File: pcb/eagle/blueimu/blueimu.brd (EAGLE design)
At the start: 50 x 73 mm, 26 parts, among them IC1 ICL7665CPA, IC2 ATMEGA328P, IC3 LP2950Z, J1 22-27-2021-02, Q1 IRL3803, Q2 7.3728MHz

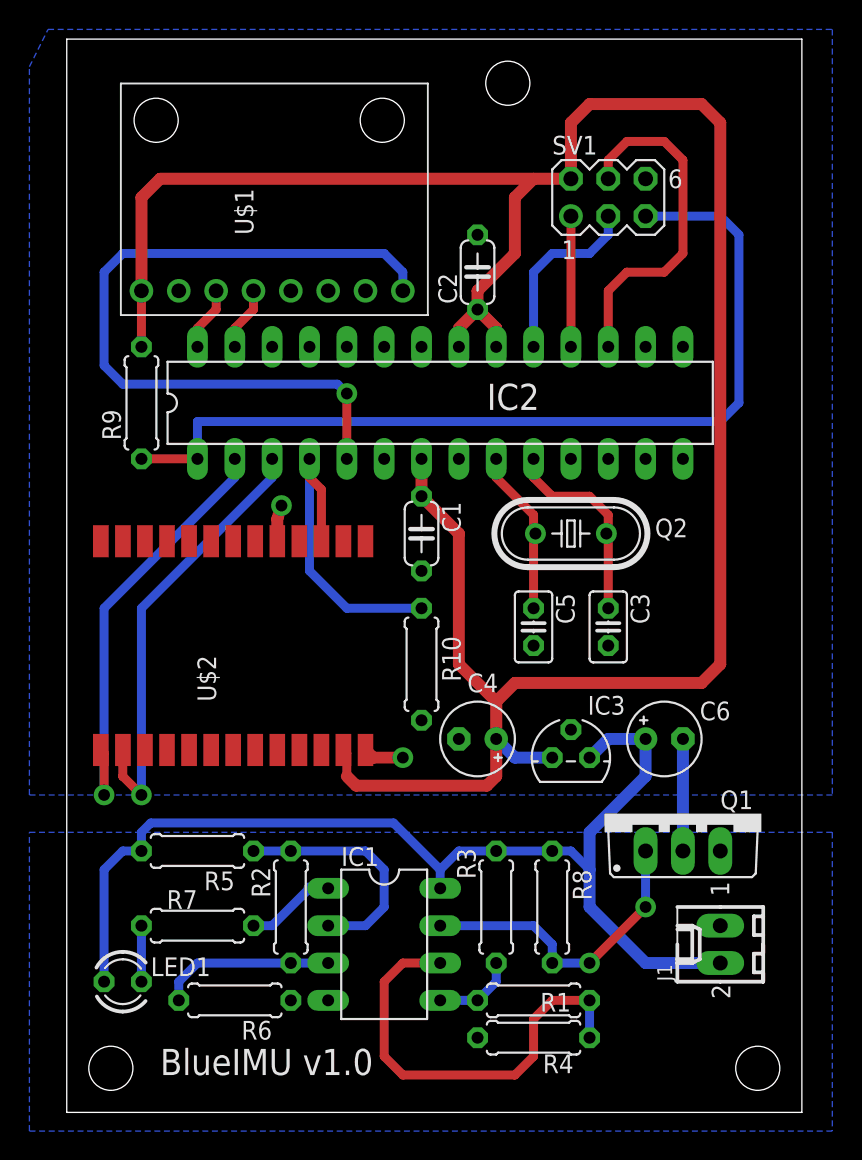
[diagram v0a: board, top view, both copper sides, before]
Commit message: Cosmetic changes to schematics and board layout
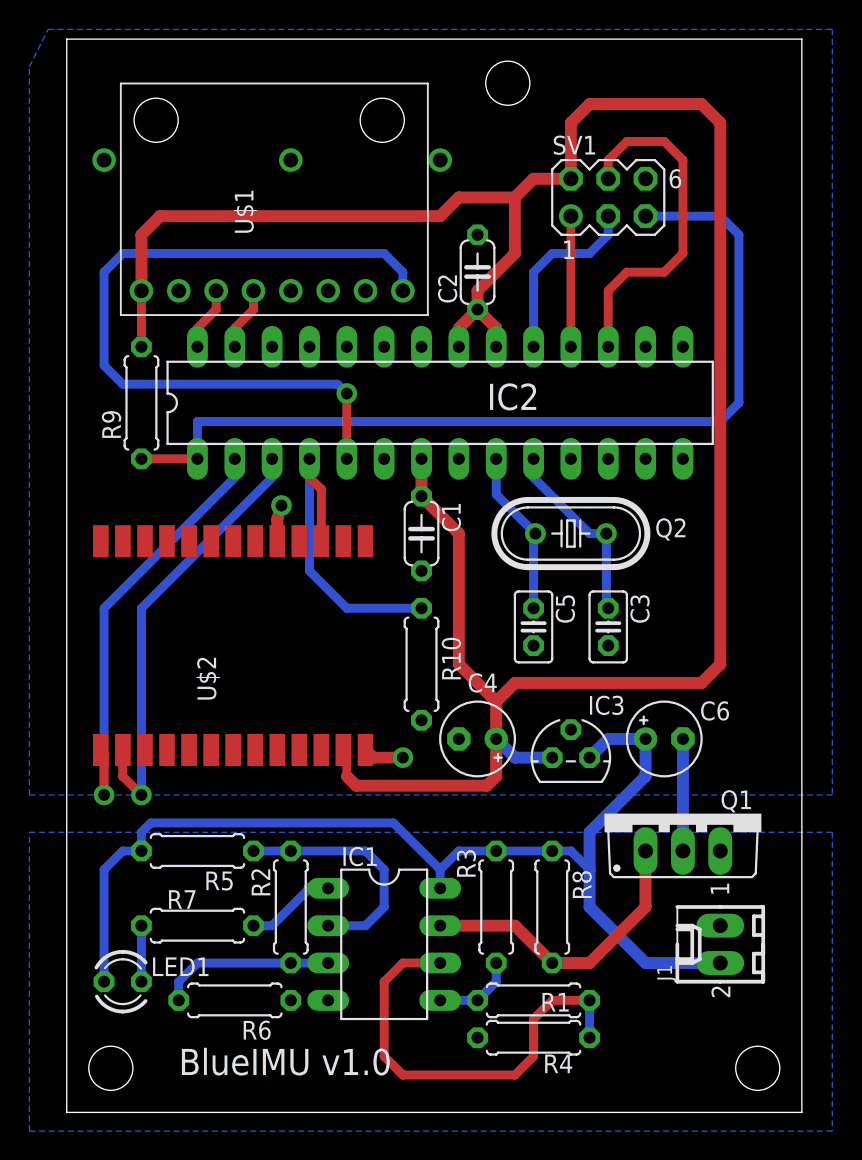
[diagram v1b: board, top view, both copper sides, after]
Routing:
- net +3V3: track 165.2 -> 162.0 mm
- net N$10: track 13.8 -> 12.9 mm
- net N$9: track 21.2 -> 20.4 mm, vias 2 -> 0
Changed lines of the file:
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@@
 <setting verticaltext="up"/>
 </settings>
-<grid distance="1270" unitdist="mic" unit="mil" style="lines" multiple="1" display="yes" altdistance="0.635" altunitdist="mm" altunit="mm"/>
+<grid distance="1.27" unitdist="mm" unit="mm" style="lines" multiple="1" display="yes" altdistance="0.635" altunitdist="mm" altunit="mm"/>
 <layers>
 <layer number="1" name="Top" color="4" fill="1" visible="yes" active="yes"/>
@@
 <hole x="3" y="3" drill="3"/>
 <hole x="47" y="3" drill="3"/>
-<circle x="47" y="3" radius="3" width="0" layer="42"/>
-<circle x="3" y="3" radius="3" width="0" layer="42"/>
+<circle x="47" y="3" radius="3.3" width="0" layer="42"/>
+<circle x="3" y="3" radius="3.3" width="0" layer="42"/>
 <hole x="30" y="70" drill="3"/>
-<circle x="30" y="70" radius="3" width="0" layer="42"/>
-<text x="6.35" y="2.54" size="1.778" layer="21">BlueIMU v1.0</text>
+<circle x="30" y="70" radius="3.3" width="0" layer="42"/>
+<text x="7.62" y="2.54" size="1.778" layer="21">BlueIMU v1.0</text>
 </plain>
 <attributes>
@@
 <contactref element="Q1" pad="G"/>
 <contactref element="R8" pad="2"/>
-<wire x1="25.4" y1="12.7" x2="31.75" y2="12.7" width="0.6096" layer="16"/>
-<wire x1="31.75" y1="12.7" x2="33.02" y2="11.43" width="0.6096" layer="16"/>
-<wire x1="33.02" y1="11.43" x2="33.02" y2="10.16" width="0.6096" layer="16"/>
-<via x="35.56" y="10.16" extent="1-16" drill="0.8"/>
-<wire x1="33.02" y1="10.16" x2="35.56" y2="10.16" width="0.6096" layer="16"/>
-<via x="39.37" y="13.97" extent="1-16" drill="0.8"/>
-<wire x1="39.37" y1="17.78" x2="39.37" y2="13.97" width="0.6096" layer="16"/>
-<wire x1="35.56" y1="10.16" x2="39.37" y2="13.97" width="0.6096" layer="1"/>
+<wire x1="25.4" y1="12.7" x2="30.48" y2="12.7" width="0.8128" layer="1"/>
+<wire x1="30.48" y1="12.7" x2="33.02" y2="10.16" width="0.8128" layer="1"/>
+<wire x1="33.02" y1="10.16" x2="35.56" y2="10.16" width="0.8128" layer="1"/>
+<wire x1="35.56" y1="10.16" x2="39.37" y2="13.97" width="0.8128" layer="1"/>
+<wire x1="39.37" y1="13.97" x2="39.37" y2="17.78" width="0.8128" layer="1"/>
 </signal>
 <signal name="N$12">
@@
 <wire x1="30.48" y1="62.23" x2="30.48" y2="58.42" width="0.8128" layer="1"/>
 <wire x1="5.08" y1="55.88" x2="5.08" y2="52.07" width="0.6096" layer="1"/>
-<wire x1="5.08" y1="55.88" x2="5.08" y2="62.23" width="0.8128" layer="1"/>
-<wire x1="5.08" y1="62.23" x2="6.35" y2="63.5" width="0.8128" layer="1"/>
-<wire x1="6.35" y1="63.5" x2="31.75" y2="63.5" width="0.8128" layer="1"/>
 <wire x1="29.21" y1="25.4" x2="29.21" y2="22.86" width="0.8128" layer="1"/>
 <wire x1="29.21" y1="22.86" x2="28.575" y2="22.225" width="0.8128" layer="1"/>
@@
 <wire x1="27.94" y1="54.61" x2="29.21" y2="53.34" width="0.8128" layer="1"/>
 <wire x1="29.21" y1="53.34" x2="29.21" y2="52.07" width="0.8128" layer="1"/>
+<wire x1="25.4" y1="60.96" x2="6.35" y2="60.96" width="0.8128" layer="1"/>
+<wire x1="6.35" y1="60.96" x2="5.08" y2="59.69" width="0.8128" layer="1"/>
+<wire x1="5.08" y1="59.69" x2="5.08" y2="55.88" width="0.8128" layer="1"/>
+<wire x1="25.4" y1="60.96" x2="26.67" y2="62.23" width="0.8128" layer="1"/>
+<wire x1="26.67" y1="62.23" x2="30.48" y2="62.23" width="0.8128" layer="1"/>
 </signal>
 <signal name="TXD">
@@
 </signal>
 <signal name="N$15">
-<wire x1="31.75" y1="40.64" x2="29.21" y2="43.18" width="0.6096" layer="1"/>
 <contactref element="IC2" pad="9"/>
 <contactref element="Q2" pad="1"/>
 <contactref element="C5" pad="1"/>
-<wire x1="29.21" y1="43.18" x2="29.21" y2="44.45" width="0.6096" layer="1"/>
-<wire x1="31.75" y1="34.29" x2="31.75" y2="40.64" width="0.6096" layer="1"/>
-<wire x1="31.75" y1="40.64" x2="31.877" y2="39.37" width="0" layer="19" extent="1-1"/>
+<wire x1="31.877" y1="39.37" x2="31.75" y2="39.243" width="0.6096" layer="16"/>
+<wire x1="31.75" y1="39.243" x2="31.75" y2="34.29" width="0.6096" layer="16"/>
+<wire x1="31.877" y1="39.37" x2="29.21" y2="42.037" width="0.6096" layer="16"/>
+<wire x1="29.21" y1="42.037" x2="29.21" y2="44.45" width="0.6096" layer="16"/>
 </signal>
 <signal name="N$10">
-<wire x1="36.83" y1="40.64" x2="35.56" y2="41.91" width="0.6096" layer="1"/>
-<wire x1="35.56" y1="41.91" x2="33.02" y2="41.91" width="0.6096" layer="1"/>
 <contactref element="IC2" pad="10"/>
 <contactref element="Q2" pad="2"/>
 <contactref element="C3" pad="1"/>
-<wire x1="33.02" y1="41.91" x2="31.75" y2="43.18" width="0.6096" layer="1"/>
-<wire x1="31.75" y1="43.18" x2="31.75" y2="44.45" width="0.6096" layer="1"/>
-<wire x1="36.83" y1="34.29" x2="36.83" y2="40.64" width="0.6096" layer="1"/>
-<wire x1="36.83" y1="40.64" x2="36.703" y2="39.37" width="0" layer="19" extent="1-1"/>
+<wire x1="36.83" y1="34.29" x2="36.703" y2="34.417" width="0.6096" layer="16" curve="-90"/>
+<wire x1="36.703" y1="34.417" x2="36.703" y2="39.37" width="0.6096" layer="16"/>
+<wire x1="36.703" y1="39.37" x2="35.56" y2="39.37" width="0.6096" layer="16"/>
+<wire x1="35.56" y1="39.37" x2="31.75" y2="43.18" width="0.6096" layer="16"/>
+<wire x1="31.75" y1="43.18" x2="31.75" y2="44.45" width="0.6096" layer="16"/>
+</signal>
+<signal name="N$11">
+<via x="2.54" y="64.77" extent="1-16" drill="1" shape="octagon"/>
+</signal>
+<signal name="N$14">
+<via x="25.4" y="64.77" extent="1-16" drill="1" shape="octagon"/>
+</signal>
+<signal name="N$16">
+<via x="15.24" y="64.77" extent="1-16" drill="1" shape="octagon"/>
 </signal>
 </signals>

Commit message: Added capacitor. Added Gerber files.
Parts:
- added C7: 100nF, rcl:C050-024X044
- R8: value 1M -> 470k
- moved J1 1.27 mm to (44.5, 10.2)
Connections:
- net BAT-: now also C7.2
- net N$9: now also C7.1
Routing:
- net BAT+: track 74.1 -> 74.7 mm
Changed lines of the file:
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@@
 <attribute name="VALUE" x="11.176" y="13.2588" size="1.27" layer="27" ratio="10" rot="R180"/>
 </element>
-<element name="R8" library="rcl" package="0207/7" value="1M" x="33.02" y="13.97" rot="R270"/>
+<element name="R8" library="rcl" package="0207/7" value="470k" x="33.02" y="13.97" rot="R270"/>
 <element name="SV1" library="con-lstb" package="MA03-2" value="" x="36.83" y="62.23" smashed="yes">
 <attribute name="OC_NEWARK" value="unknown" x="36.83" y="62.23" size="1.778" layer="27" display="off"/>
@@
 <attribute name="VALUE" x="35.56" y="58.039" size="1.27" layer="27" ratio="10"/>
 </element>
-<element name="J1" library="con-molex" package="6410-02" value="22-27-2021-02" x="44.45" y="11.43" rot="R90">
-<attribute name="OC_NEWARK" value="unknown" x="44.45" y="11.43" size="1.778" layer="27" rot="R90" display="off"/>
-<attribute name="MPN" value="" x="44.45" y="11.43" size="1.778" layer="27" rot="R90" display="off"/>
-<attribute name="MF" value="" x="44.45" y="11.43" size="1.778" layer="27" rot="R90" display="off"/>
-<attribute name="OC_FARNELL" value="unknown" x="44.45" y="11.43" size="1.778" layer="27" rot="R90" display="off"/>
+<element name="J1" library="con-molex" package="6410-02" value="22-27-2021-02" x="44.45" y="10.16" rot="R90">
+<attribute name="OC_NEWARK" value="unknown" x="44.45" y="10.16" size="1.778" layer="27" rot="R90" display="off"/>
+<attribute name="MPN" value="" x="44.45" y="10.16" size="1.778" layer="27" rot="R90" display="off"/>
+<attribute name="MF" value="" x="44.45" y="10.16" size="1.778" layer="27" rot="R90" display="off"/>
+<attribute name="OC_FARNELL" value="unknown" x="44.45" y="10.16" size="1.778" layer="27" rot="R90" display="off"/>
 </element>
 <element name="IC2" library="atmel" package="DIL28-3" value="ATMEGA328P" x="25.4" y="48.26" smashed="yes">
@@
 <attribute name="VALUE" x="23.5712" y="32.766" size="1.27" layer="27" ratio="10" rot="R270"/>
 </element>
+<element name="C7" library="rcl" package="C050-024X044" value="100nF" x="41.91" y="14.605" smashed="yes">
+<attribute name="NAME" x="45.466" y="14.097" size="1.27" layer="25" ratio="10"/>
+<attribute name="VALUE" x="39.751" y="11.938" size="1.27" layer="27" ratio="10"/>
+</element>
 </elements>
 <signals>
@@
 <contactref element="C6" pad="+"/>
 <contactref element="IC3" pad="3"/>
-<wire x1="44.45" y1="10.16" x2="39.37" y2="10.16" width="0.8128" layer="16"/>
-<wire x1="39.37" y1="10.16" x2="35.56" y2="13.97" width="0.8128" layer="16"/>
+<wire x1="44.45" y1="8.89" x2="40.64" y2="8.89" width="0.8128" layer="16"/>
+<wire x1="40.64" y1="8.89" x2="35.56" y2="13.97" width="0.8128" layer="16"/>
 <wire x1="35.56" y1="13.97" x2="35.56" y2="16.51" width="0.8128" layer="16"/>
 <wire x1="35.56" y1="16.51" x2="34.29" y2="17.78" width="0.6096" layer="16"/>
@@
 </polygon>
 <contactref element="J1" pad="1"/>
+<contactref element="C7" pad="2"/>
 </signal>
 <signal name="N$3">
@@
 <wire x1="30.48" y1="12.7" x2="33.02" y2="10.16" width="0.8128" layer="1"/>
 <wire x1="33.02" y1="10.16" x2="35.56" y2="10.16" width="0.8128" layer="1"/>
-<wire x1="35.56" y1="10.16" x2="39.37" y2="13.97" width="0.8128" layer="1"/>
-<wire x1="39.37" y1="13.97" x2="39.37" y2="17.78" width="0.8128" layer="1"/>
+<wire x1="35.56" y1="10.16" x2="39.37" y2="14.605" width="0.8128" layer="1"/>
+<wire x1="39.37" y1="14.605" x2="39.37" y2="17.78" width="0.8128" layer="1"/>
+<contactref element="C7" pad="1"/>
 </signal>
 <signal name="N$12">
